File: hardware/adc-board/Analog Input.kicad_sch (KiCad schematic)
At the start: 59 parts, among them J1 BHR-44-HUA, U1 Opamp_Quad_Generic, U10 MCP1501T-20E/CHY, U2 Opamp_Quad_Generic, U29 AP2114HA-3.3TRG1, U3 Opamp_Quad_Generic, U4 Opamp_Quad_Generic, U5 Opamp_Quad_Generic, U6 Opamp_Quad_Generic

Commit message: Unified ground nets in schematic and layout.
* Rearranged the layers that pours are on.
* Added the keep-out zone separating analog and
  digital areas from each other.
* Tightened up placement of decoupling capacitors.
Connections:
- net GNDA renamed GND
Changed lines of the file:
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@@
   (junction (at 17.78 152.4) (diameter 0) (color 0 0 0 0)
   )
+  (junction (at 151.13 237.49) (diameter 0) (color 0 0 0 0)
+  )
   (junction (at 172.72 90.17) (diameter 0) (color 0 0 0 0)
   )
@@
   )
   (junction (at 322.58 154.94) (diameter 0) (color 0 0 0 0)
-  )
-  (junction (at 152.4 237.49) (diameter 0) (color 0 0 0 0)
   )
   (junction (at 242.57 195.58) (diameter 0) (color 0 0 0 0)
@@
     (stroke (width 0) (type default) (color 0 0 0 0))
   )
+  (wire (pts (xy 151.13 237.49) (xy 152.4 237.49))
+    (stroke (width 0) (type default) (color 0 0 0 0))
+  )
   (wire (pts (xy 190.5 173.99) (xy 189.23 173.99))
     (stroke (width 0) (type default) (color 0 0 0 0))
@@
     (stroke (width 0) (type default) (color 0 0 0 0))
   )
-  (wire (pts (xy 149.86 237.49) (xy 152.4 237.49))
+  (wire (pts (xy 149.86 237.49) (xy 151.13 237.49))
     (stroke (width 0) (type default) (color 0 0 0 0))
   )
@@
     (pin "1")
     (pin "2")
-  )
-  (symbol (lib_id "power:GNDA") (at 46.99 180.34 0) (unit 1)
-    (in_bom yes) (on_board yes)
-    (property "Reference" "#PWR0111" (id 0) (at 46.99 186.69 0)
-      (effects (font (size 1.27 1.27)) hide)
-    )
-    (property "Value" "GNDA" (id 1) (at 47.117 184.7342 0))
-    (property "Footprint" "" (id 2) (at 46.99 180.34 0)
-      (effects (font (size 1.27 1.27)) hide)
-    )
-    (property "Datasheet" "" (id 3) (at 46.99 180.34 0)
-      (effects (font (size 1.27 1.27)) hide)
-    )
-    (pin "1")
   )
   (symbol (lib_id "Connector_Generic:Conn_02x22_Odd_Even") (at 25.4 137.16 180) (unit 1)
@@
     (pin "14")
   )
-  (symbol (lib_id "power:GNDA") (at 111.76 35.56 0) (unit 1)
-    (in_bom yes) (on_board yes)
-    (property "Reference" "#PWR0124" (id 0) (at 111.76 41.91 0)
-      (effects (font (size 1.27 1.27)) hide)
-    )
-    (property "Value" "GNDA" (id 1) (at 111.887 39.9542 0))
-    (property "Footprint" "" (id 2) (at 111.76 35.56 0)
-      (effects (font (size 1.27 1.27)) hide)
-    )
-    (property "Datasheet" "" (id 3) (at 111.76 35.56 0)
-      (effects (font (size 1.27 1.27)) hide)
-    )
-    (pin "1")
-  )
-  (symbol (lib_id "power:GNDA") (at 162.56 35.56 0) (unit 1)
-    (in_bom yes) (on_board yes)
-    (property "Reference" "#PWR0125" (id 0) (at 162.56 41.91 0)
-      (effects (font (size 1.27 1.27)) hide)
-    )
-    (property "Value" "GNDA" (id 1) (at 162.687 39.9542 0))
-    (property "Footprint" "" (id 2) (at 162.56 35.56 0)
-      (effects (font (size 1.27 1.27)) hide)
-    )
-    (property "Datasheet" "" (id 3) (at 162.56 35.56 0)
-      (effects (font (size 1.27 1.27)) hide)
-    )
-    (pin "1")
-  )
   (symbol (lib_id "MCP1501-ECHY:MCP1501-ECHY") (at 125.73 234.95 0) (unit 1)
     (in_bom yes) (on_board yes)
@@
     (pin "4")
   )
-  (symbol (lib_id "power:GNDA") (at 152.4 237.49 0) (unit 1)
-    (in_bom yes) (on_board yes)
-    (property "Reference" "#PWR0119" (id 0) (at 152.4 243.84 0)
-      (effects (font (size 1.27 1.27)) hide)
-    )
-    (property "Value" "GNDA" (id 1) (at 152.527 241.8842 0))
-    (property "Footprint" "" (id 2) (at 152.4 237.49 0)
-      (effects (font (size 1.27 1.27)) hide)
-    )
-    (property "Datasheet" "" (id 3) (at 152.4 237.49 0)
-      (effects (font (size 1.27 1.27)) hide)
-    )
-    (pin "1")
-  )
-  (symbol (lib_id "power:GNDA") (at 149.86 132.08 0) (unit 1)
-    (in_bom yes) (on_board yes)
-    (property "Reference" "#PWR0141" (id 0) (at 149.86 138.43 0)
-      (effects (font (size 1.27 1.27)) hide)
-    )
-    (property "Value" "GNDA" (id 1) (at 149.987 136.4742 0))
-    (property "Footprint" "" (id 2) (at 149.86 132.08 0)
-      (effects (font (size 1.27 1.27)) hide)
-    )
-    (property "Datasheet" "" (id 3) (at 149.86 132.08 0)
-      (effects (font (size 1.27 1.27)) hide)
-    )
-    (pin "1")
-  )
   (symbol (lib_id "power:+3.3VA") (at 123.19 78.74 0) (unit 1)
     (in_bom yes) (on_board yes)
@@
     (pin "3")
   )
-  (symbol (lib_id "power:GNDA") (at 125.73 175.26 0) (unit 1)
-    (in_bom yes) (on_board yes)
-    (property "Reference" "#PWR0130" (id 0) (at 125.73 181.61 0)
-      (effects (font (size 1.27 1.27)) hide)
-    )
-    (property "Value" "GNDA" (id 1) (at 125.857 179.6542 0))
-    (property "Footprint" "" (id 2) (at 125.73 175.26 0)
-      (effects (font (size 1.27 1.27)) hide)
-    )
-    (property "Datasheet" "" (id 3) (at 125.73 175.26 0)
-      (effects (font (size 1.27 1.27)) hide)
-    )
-    (pin "1")
-  )
   (symbol (lib_id "power:+3.3VA") (at 144.78 165.1 0) (unit 1)
     (in_bom yes) (on_board yes)
@@
     (pin "2")
   )
-  (symbol (lib_id "power:GNDA") (at 102.87 242.57 0) (unit 1)
-    (in_bom yes) (on_board yes)
-    (property "Reference" "#PWR0126" (id 0) (at 102.87 248.92 0)
-      (effects (font (size 1.27 1.27)) hide)
-    )
-    (property "Value" "GNDA" (id 1) (at 102.997 246.9642 0))
-    (property "Footprint" "" (id 2) (at 102.87 242.57 0)
-      (effects (font (size 1.27 1.27)) hide)
-    )
-    (property "Datasheet" "" (id 3) (at 102.87 242.57 0)
-      (effects (font (size 1.27 1.27)) hide)
-    )
-    (pin "1")
-  )
   (symbol (lib_id "Device:C_Small") (at 93.98 237.49 0) (unit 1)
     (in_bom yes) (on_board yes)
@@
       (effects (font (size 1.27 1.27)) hide)
     )
+    (pin "1")
+  )
+  (symbol (lib_id "power:GND") (at 125.73 175.26 0) (unit 1)
+    (in_bom yes) (on_board yes) (fields_autoplaced)
+    (property "Reference" "#PWR0139" (id 0) (at 125.73 181.61 0)
+      (effects (font (size 1.27 1.27)) hide)
+    )
+    (property "Value" "GND" (id 1) (at 125.73 179.8225 0))
+    (property "Footprint" "" (id 2) (at 125.73 175.26 0)
+      (effects (font (size 1.27 1.27)) hide)
+    )
+    (property "Datasheet" "" (id 3) (at 125.73 175.26 0)
+      (effects (font (size 1.27 1.27)) hide)
+    )
+    (pin "1")
+  )
+  (symbol (lib_id "power:GND") (at 46.99 180.34 0) (unit 1)
+    (in_bom yes) (on_board yes) (fields_autoplaced)
+    (property "Reference" "#PWR0134" (id 0) (at 46.99 186.69 0)
+      (effects (font (size 1.27 1.27)) hide)
+    )
+    (property "Value" "GND" (id 1) (at 46.99 184.9025 0))
+    (property "Footprint" "" (id 2) (at 46.99 180.34 0)
+      (effects (font (size 1.27 1.27)) hide)
+    )
+    (property "Datasheet" "" (id 3) (at 46.99 180.34 0)
+      (effects (font (size 1.27 1.27)) hide)
+    )
+    (pin "1")
+  )
+  (symbol (lib_id "power:GND") (at 111.76 35.56 0) (unit 1)
+    (in_bom yes) (on_board yes) (fields_autoplaced)
+    (property "Reference" "#PWR0138" (id 0) (at 111.76 41.91 0)
+      (effects (font (size 1.27 1.27)) hide)
+    )
+    (property "Value" "GND" (id 1) (at 111.76 40.1225 0))
+    (property "Footprint" "" (id 2) (at 111.76 35.56 0)
+      (effects (font (size 1.27 1.27)) hide)
+    )
+    (property "Datasheet" "" (id 3) (at 111.76 35.56 0)
+      (effects (font (size 1.27 1.27)) hide)
+    )
+    (pin "1")
+  )
+  (symbol (lib_id "power:GND") (at 149.86 132.08 0) (unit 1)
+    (in_bom yes) (on_board yes) (fields_autoplaced)
+    (property "Reference" "#PWR0125" (id 0) (at 149.86 138.43 0)
+      (effects (font (size 1.27 1.27)) hide)
+    )
+    (property "Value" "GND" (id 1) (at 149.86 136.6425 0))
+    (property "Footprint" "" (id 2) (at 149.86 132.08 0)
+      (effects (font (size 1.27 1.27)) hide)
+    )
+    (property "Datasheet" "" (id 3) (at 149.86 132.08 0)
+      (effects (font (size 1.27 1.27)) hide)
+    )
+    (pin "1")
+  )
+  (symbol (lib_id "power:GND") (at 102.87 242.57 0) (unit 1)
+    (in_bom yes) (on_board yes) (fields_autoplaced)
+    (property "Reference" "#PWR0126" (id 0) (at 102.87 248.92 0)
+      (effects (font (size 1.27 1.27)) hide)
+    )
+    (property "Value" "GND" (id 1) (at 102.87 247.1325 0))
+    (property "Footprint" "" (id 2) (at 102.87 242.57 0)
+      (effects (font (size 1.27 1.27)) hide)
+    )
+    (property "Datasheet" "" (id 3) (at 102.87 242.57 0)
+      (effects (font (size 1.27 1.27)) hide)
+    )
+    (pin "1")
+  )
+  (symbol (lib_id "power:GND") (at 151.13 237.49 0) (unit 1)
+    (in_bom yes) (on_board yes) (fields_autoplaced)
+    (property "Reference" "#PWR0130" (id 0) (at 151.13 243.84 0)
+      (effects (font (size 1.27 1.27)) hide)
+    )
+    (property "Value" "GND" (id 1) (at 151.13 242.0525 0))
+    (property "Footprint" "" (id 2) (at 151.13 237.49 0)
+      (effects (font (size 1.27 1.27)) hide)
+    )
+    (property "Datasheet" "" (id 3) (at 151.13 237.49 0)
+      (effects (font (size 1.27 1.27)) hide)
+    )
+    (pin "1")
+  )
+  (symbol (lib_id "power:GND") (at 162.56 35.56 0) (unit 1)
+    (in_bom yes) (on_board yes) (fields_autoplaced)
+    (property "Reference" "#PWR0136" (id 0) (at 162.56 41.91 0)
+      (effects (font (size 1.27 1.27)) hide)
+    )
+    (property "Value" "GND" (id 1) (at 162.56 40.1225 0))
+    (property "Footprint" "" (id 2) (at 162.56 35.56 0)
+      (effects (font (size 1.27 1.27)) hide)
+    )
+    (property "Datasheet" "" (id 3) (at 162.56 35.56 0)
+      (effects (font (size 1.27 1.27)) hide)
+    )

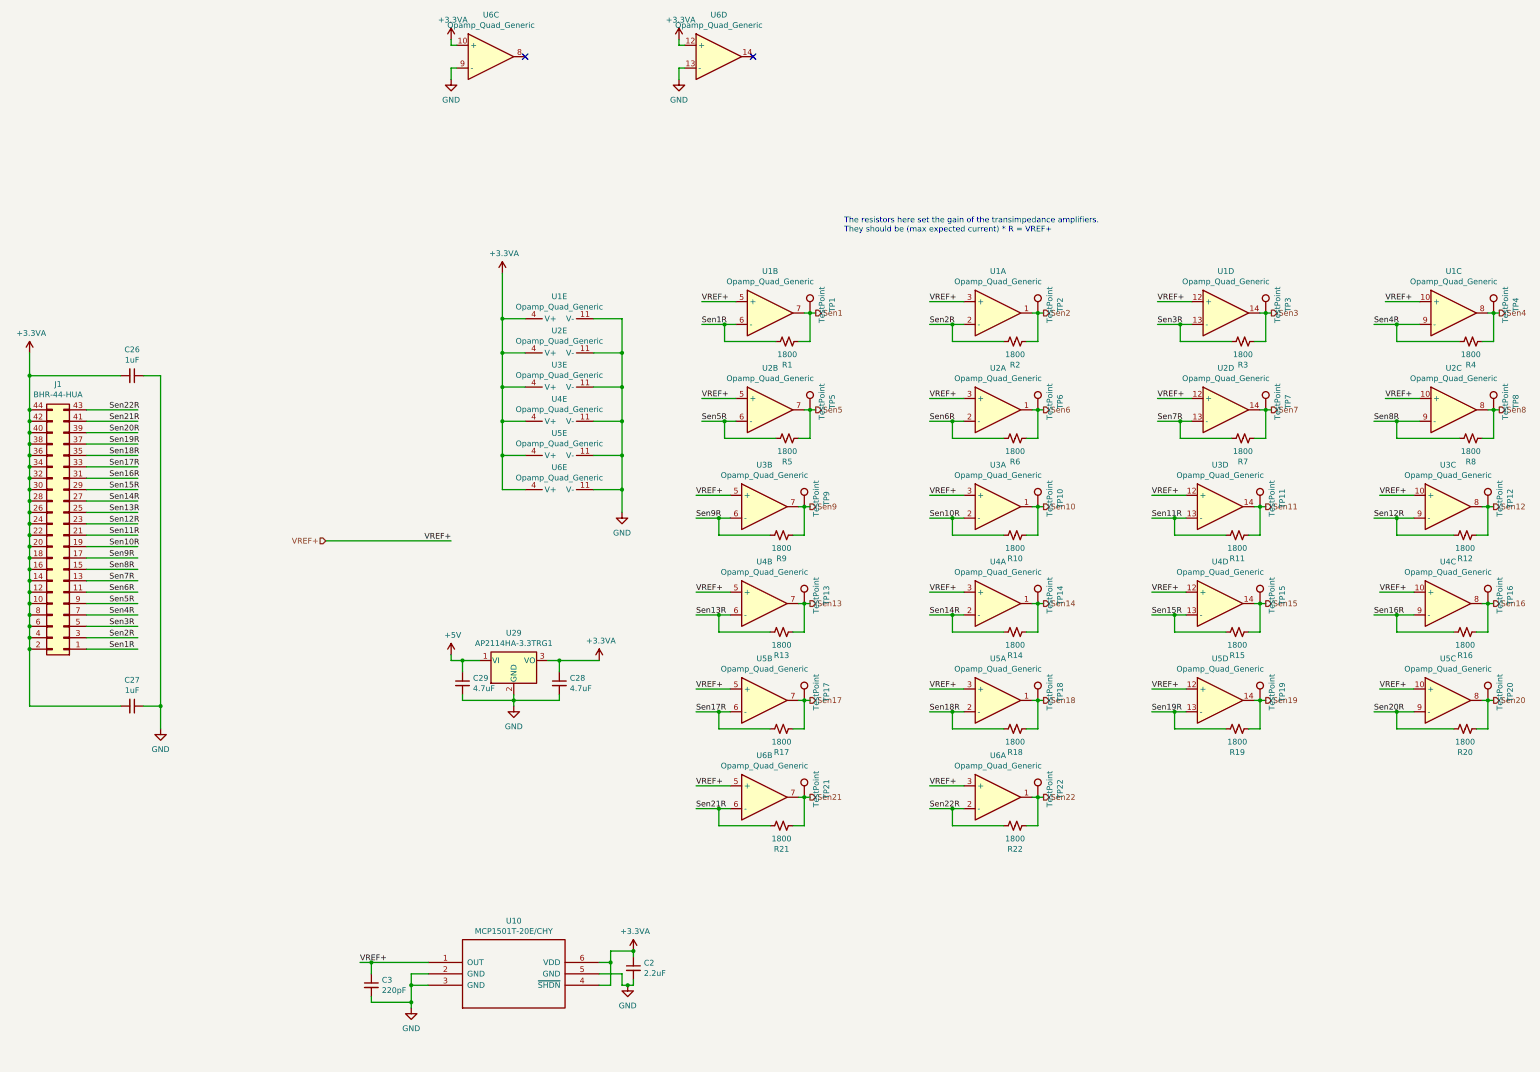
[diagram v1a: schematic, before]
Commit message: More ADC board rev 3 changes, per issue #47
* 4.5V regulator for phototransistors
* new 3.3V regulator for analog section
* new 2.0V precision voltage reference
* Analog voltages and their distribution rearranged
* Tidied up traces on the left hand side, everything is nice and curvy now
* Adjusted USB ESD protection to be optional and/or support other parts
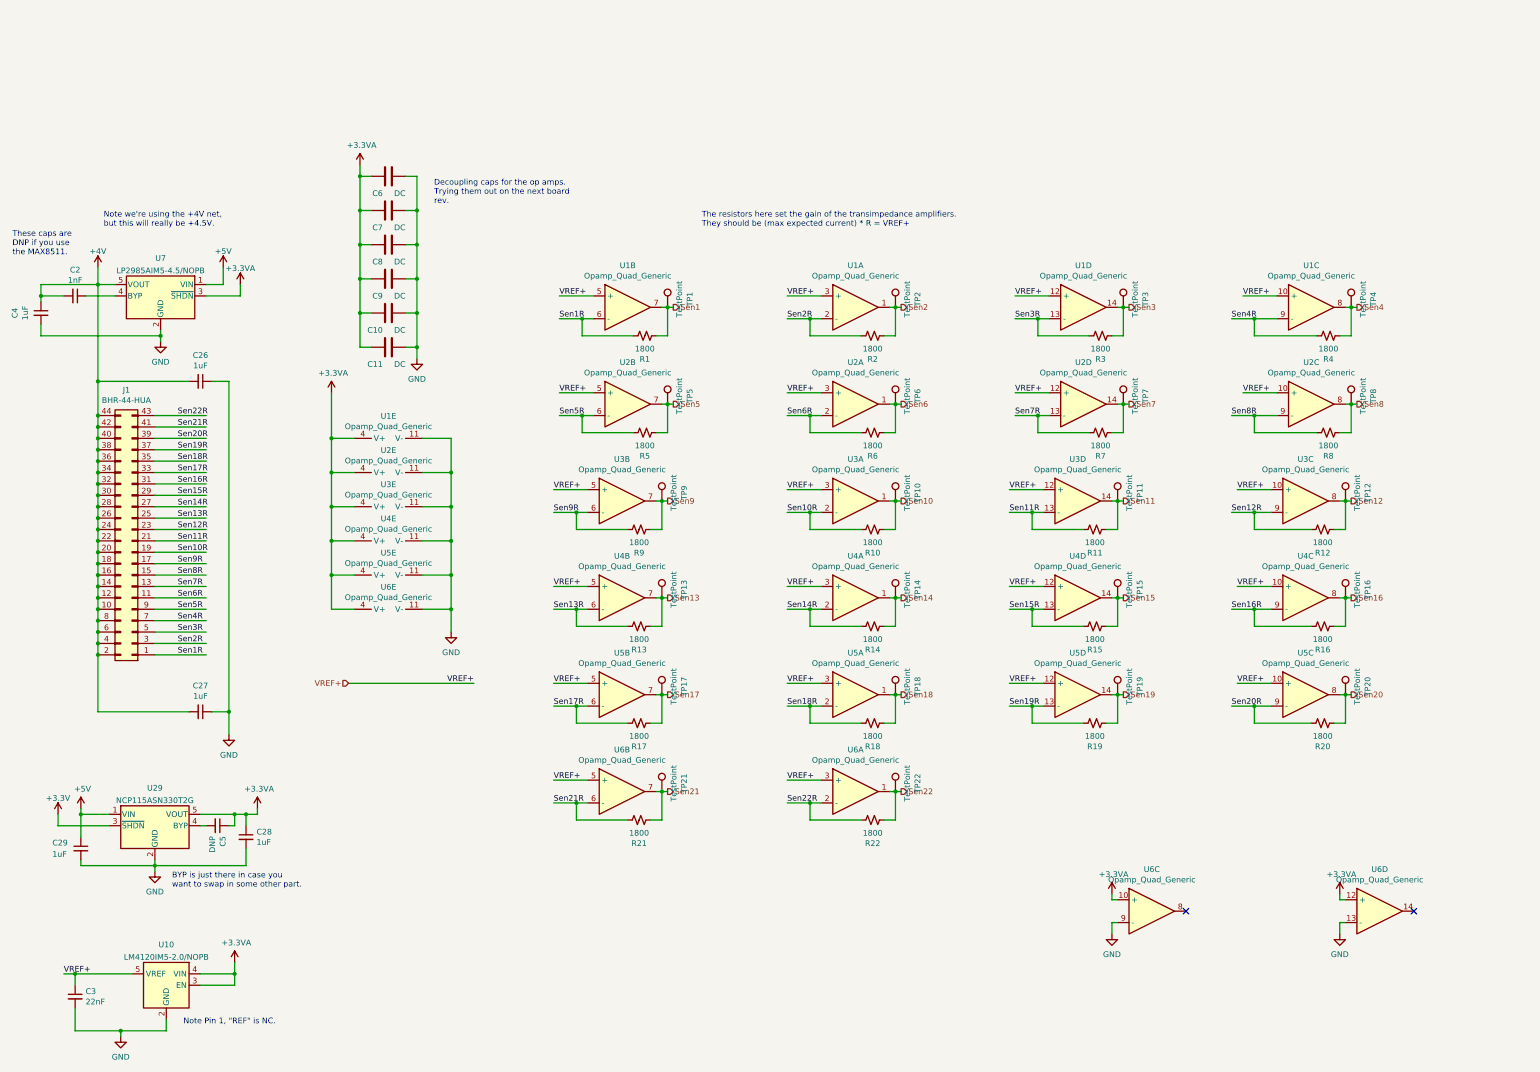
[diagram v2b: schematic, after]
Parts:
- removed U10: MCP1501T-20E/CHY, TO_SOT_Packages_SMD:SOT-23-6_Handsoldering, symbol MCP1501-ECHY:MCP1501-ECHY
- removed U29: AP2114HA-3.3TRG1, TO_SOT_Packages_SMD:SOT-223-3_TabPin2, symbol Regulator_Linear:AP7361C-33E
- added C10, C11, C6, C7, C8, C9: DC, Capacitor_SMD:C_0805_2012Metric, symbol Device:C
- added C4: 1uF, Capacitor_SMD:C_0805_2012Metric, symbol Device:C_Small
- added C5: DNP, Capacitor_SMD:C_0805_2012Metric, symbol Device:C_Small
- added U10: LM4120IM5-2.0/NOPB, Package_TO_SOT_SMD:SOT-23-5, symbol Reference_Voltage:LM4128
- added U29: NCP115ASN330T2G, Package_TO_SOT_SMD:SOT-23-5, symbol Regulator_Linear:APE8865U5-12-HF-3
- added U7: LP2985AIM5-4.5/NOPB, Package_TO_SOT_SMD:SOT-23-5, symbol Regulator_Linear:APE8865U5-12-HF-3
- C2: value 2.2uF -> 1nF; footprint Capacitors_SMD:C_0805 -> Capacitor_SMD:C_0805_2012Metric
- C26, C27: footprint Capacitors_SMD:C_0805 -> Capacitor_SMD:C_0805_2012Metric
- C28, C29: value 4.7uF -> 1uF; footprint Capacitors_SMD:C_0805 -> Capacitor_SMD:C_0805_2012Metric
- C3: value 220pF -> 22nF; footprint Capacitors_SMD:C_0805 -> Capacitor_SMD:C_0805_2012Metric
- R1, R10, R11, R12, R13, R14, R15, R16, R17, R18, R19, R2, R20, R21, R22, R3, R4, R5, R6, R7, R8, R9: footprint Resistors_SMD:R_0805 -> Resistor_SMD:R_0805_2012Metric
- TP1, TP10, TP11, TP12, TP13, TP14, TP15, TP16, TP17, TP18, TP19, TP2, TP20, TP21, TP22, TP3, TP4, TP5, TP6, TP7, TP8, TP9: footprint Testpoint:TestPoint_Pad_D1.0mm -> TestPoint:TestPoint_Pad_D1.0mm
- U1, U2, U3, U4, U5, U6: footprint Housings_SSOP:TSSOP-14_4.4x5mm_Pitch0.65mm -> Package_SO:TSSOP-14_4.4x5mm_P0.65mm
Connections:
- net +3.3VA: now also C10.1, C11.1, C5.1, C6.1, C7.1, C8.1, C9.1, U10.3 (EN), U10.4 (VIN), U29.5 (VOUT), U7.3 (~{SHDN}); no longer C2.1, C26.2, C27.2, J1.10 (Pin_10), J1.12 (Pin_12), J1.14 (Pin_14), J1.16 (Pin_16), J1.18 (Pin_18), J1.2 (Pin_2), J1.20 (Pin_20), J1.22 (Pin_22), J1.24 (Pin_24), J1.26 (Pin_26), J1.28 (Pin_28), J1.30 (Pin_30), J1.32 (Pin_32), J1.34 (Pin_34), J1.36 (Pin_36), J1.38 (Pin_38), J1.4 (Pin_4), J1.40 (Pin_40), J1.42 (Pin_42), J1.44 (Pin_44), J1.6 (Pin_6), J1.8 (Pin_8)
- net +5V: now also U29.1 (VIN), U7.1 (VIN)
- net GND: now also C10.2, C11.2, C4.2, C6.2, C7.2, C8.2, C9.2, U10.2 (GND), U29.2 (GND), U7.2 (GND); no longer C2.2
- net VREF+: now also U10.5 (VREF)
- new net: C2.1, U7.4 (BYP)
- new net: C5.2, U29.4 (BYP)
- new net +3V3: U29.3 (~{SHDN})
- new net +4V: C2.2, C26.2, C27.2, C4.1, J1.10 (Pin_10), J1.12 (Pin_12), J1.14 (Pin_14), J1.16 (Pin_16), J1.18 (Pin_18), J1.2 (Pin_2), J1.20 (Pin_20), J1.22 (Pin_22), J1.24 (Pin_24), J1.26 (Pin_26), J1.28 (Pin_28), J1.30 (Pin_30), J1.32 (Pin_32), J1.34 (Pin_34), J1.36 (Pin_36), J1.38 (Pin_38), J1.4 (Pin_4), J1.40 (Pin_40), J1.42 (Pin_42), J1.44 (Pin_44), J1.6 (Pin_6), J1.8 (Pin_8), U7.5 (VOUT)
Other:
- note added: "BYP is just there in case you want to swap in some other part."
- note added: "Decoupling caps for the op amps. Trying them out on the next board rev."
- note added: "Note Pin 1, "REF" is NC."
- note added: "Note we're using the +4V net, but this will really be +4.5V."
- note added: "These caps are DNP if you use the MAX8511."
- moved on the sheet: C26, C27, C28, C29, C3, J1, R1, R10, R11, R12, R13, R14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
